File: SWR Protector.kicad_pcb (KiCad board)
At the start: 2 copper layers, 82.7 x 56.6 mm, 28 parts, among them J1 Barrel_Jack, J2 antenna, J3 Conn_02x03, J4 transceiver, J5 Barrel_Jack, K1 ATX209, Q1 2N3904, T1 1:12, T2 1:12, U1 LM78L05_TO92, U2 LM358

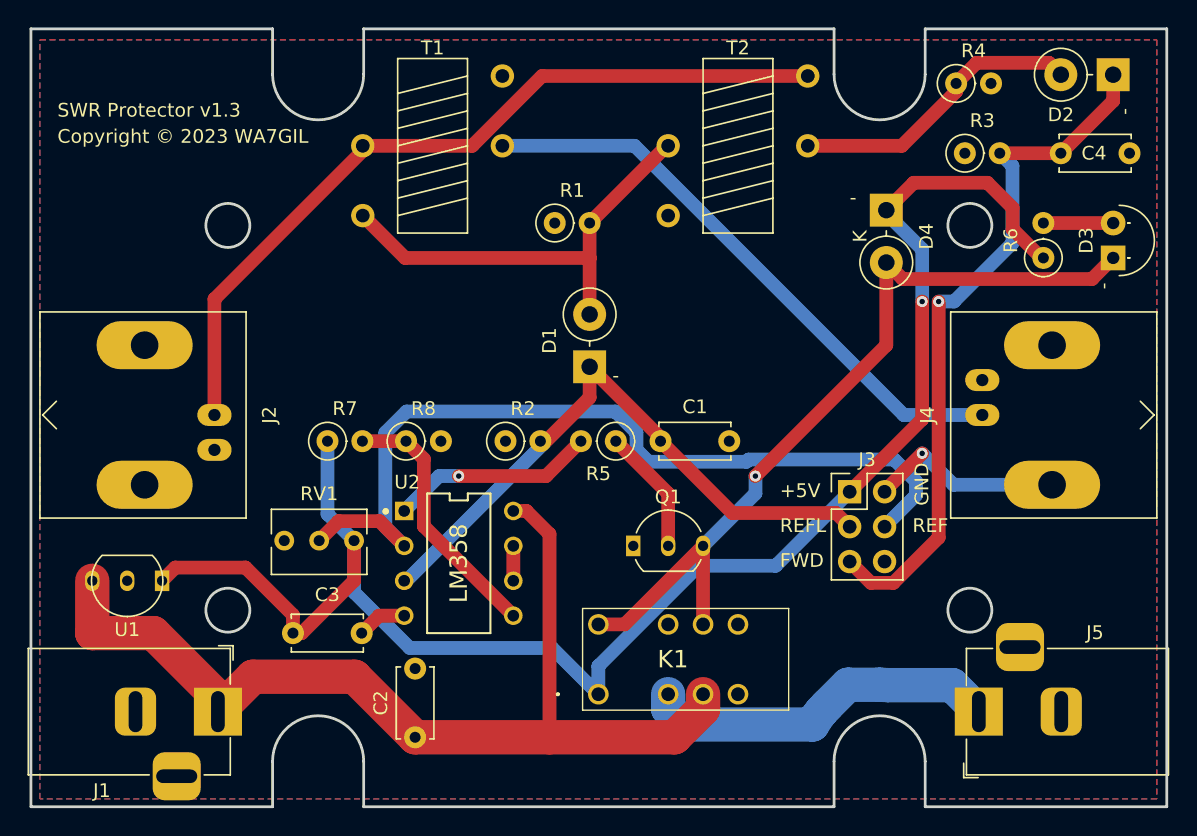
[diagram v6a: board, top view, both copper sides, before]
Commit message: The George Option complete. George asked for a buzzer when relay trips.  Used 12V part w/ same footprint. That thing is HUGE.  I can see already I want a jumper to disable it after I build one to test.
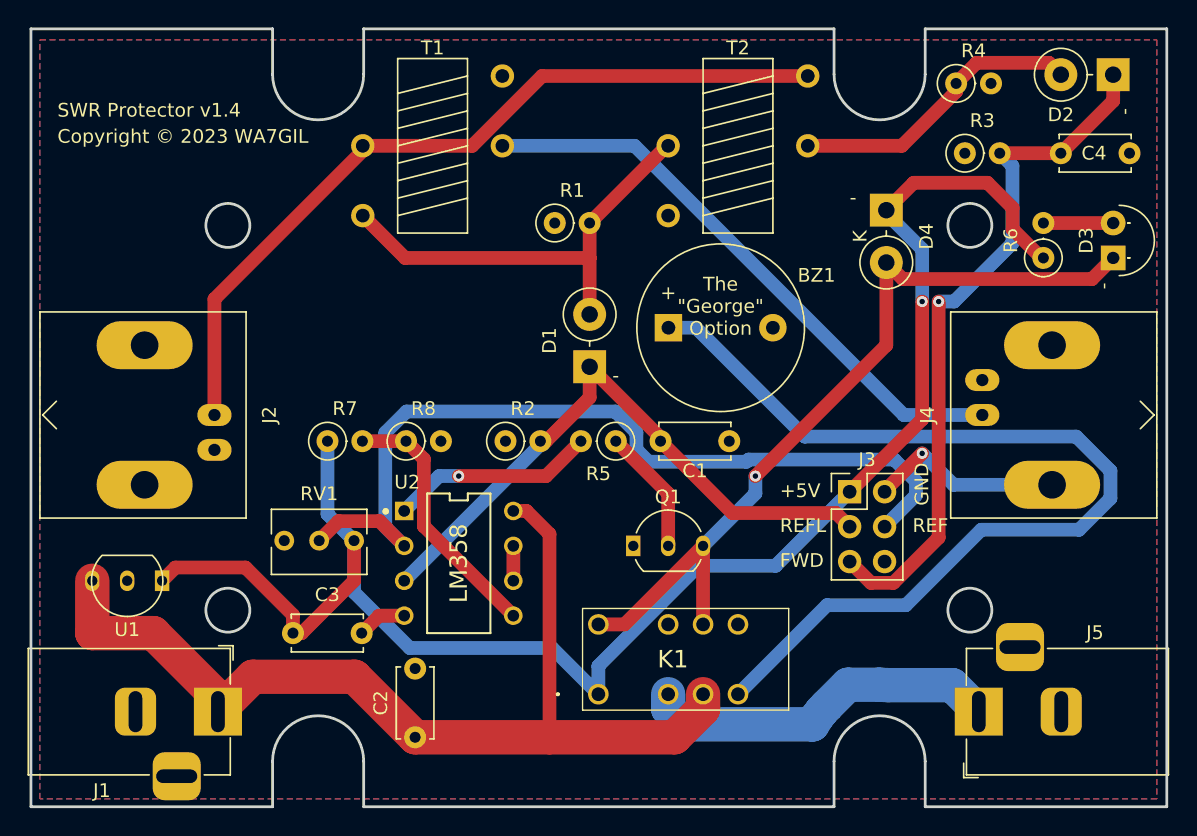
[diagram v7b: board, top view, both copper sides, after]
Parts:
- added BZ1: Buzzer, Buzzer_Beeper:Buzzer_12x9.5RM7.6, F.Cu at (160.0, 96.5)
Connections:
- K1 pad 5: unconnected-(K1-NO_1-Pad5) -> Net-(BZ1--)
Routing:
- net Net-(BZ1--): track 0.00 -> 71.5 mm
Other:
- board text added: "SWR Protector v1.4"
- board text added: "The {dblquote}George{dblquote} Option"
- board text removed: "SWR Protector v1.3"

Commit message: add jumper to disable George buzzer
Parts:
- added J6: Conn_01x02_Pin, Connector_PinHeader_2.54mm:PinHeader_1x02_P2.54mm_Vertical, F.Cu at (172.7, 104.1)
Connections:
- K1 pad 5: Net-(BZ1--) -> Net-(J6-Pin_2)
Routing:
- net Net-(BZ1--): track 71.5 -> 15.8 mm
- net Net-(J6-Pin_2): track 0.00 -> 53.1 mm
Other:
- board text added: "SWR Protector v1.5"
- board text removed: "SWR Protector v1.4"
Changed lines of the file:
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@@
     (title "SWR Protector WA7GIL")
     (date "2023-05-28")
-    (rev "v1.4")
+    (rev "v1.5")
   )
   (layers
@@
   (net 19 "unconnected-(J3-Pin_6-Pad6)")
   (net 20 "Net-(BZ1--)")
+  (net 21 "Net-(J6-Pin_2)")
   (footprint "Capacitor_THT:C_Disc_D5.0mm_W2.5mm_P5.00mm" (layer "F.Cu")
     (at 188.595 83.82)
@@
       (net 5 "+12V") (pinfunction "COM_1") (pintype "passive"))
     (pad "5" thru_hole circle (at 10.16 0) (size 1.5 1.5) (drill 1) (layers "*.Cu" "*.Mask")
-      (net 20 "Net-(BZ1--)") (pinfunction "NO_1") (pintype "passive"))
+      (net 21 "Net-(J6-Pin_2)") (pinfunction "NO_1") (pintype "passive"))
     (pad "8" thru_hole circle (at 10.16 -5.08) (size 1.5 1.5) (drill 1) (layers "*.Cu" "*.Mask")
       (net 2 "GND") (pinfunction "NO_2") (pintype "passive"))
@@
       (net 10 "Net-(J2-In)") (pinfunction "SB") (pintype "passive"))
   )
+  (footprint "Connector_PinHeader_2.54mm:PinHeader_1x02_P2.54mm_Vertical" (layer "F.Cu")
+    (at 172.715 104.14 90)
+    (descr "Through hole straight pin header, 1x02, 2.54mm pitch, single row")
+    (tags "Through hole pin header THT 1x02 2.54mm single row")
+    (property "Sheetfile" "SWR Protector.kicad_sch")
+    (property "Sheetname" "")
+    (property "ki_description" "Generic connector, single row, 01x02, script generated")
+    (property "ki_keywords" "connector")
+    (attr through_hole)
+    (fp_text reference "J6" (at 0 -2.33 90) (layer "F.SilkS")
+        (effects (font (size 1 1) (thickness 0.15)))
+    )
+    (fp_text value "Conn_01x02_Pin" (at 0 4.87 90) (layer "F.Fab")
+        (effects (font (size 1 1) (thickness 0.15)))
+    )
+    (fp_text user "${REFERENCE}" (at 0 1.27) (layer "F.Fab")
+        (effects (font (size 1 1) (thickness 0.15)))
+    )
+    (fp_line (start -1.33 -1.33) (end 0 -1.33)
+      (stroke (width 0.12) (type solid)) (layer "F.SilkS"))
+    (fp_line (start -1.33 0) (end -1.33 -1.33)
+      (stroke (width 0.12) (type solid)) (layer "F.SilkS"))
+    (fp_line (start -1.33 1.27) (end -1.33 3.87)
+      (stroke (width 0.12) (type solid)) (layer "F.SilkS"))
+    (fp_line (start -1.33 1.27) (end 1.33 1.27)
+      (stroke (width 0.12) (type solid)) (layer "F.SilkS"))
+    (fp_line (start -1.33 3.87) (end 1.33 3.87)
+      (stroke (width 0.12) (type solid)) (layer "F.SilkS"))
+    (fp_line (start 1.33 1.27) (end 1.33 3.87)
+      (stroke (width 0.12) (type solid)) (layer "F.SilkS"))
+    (fp_line (start -1.8 -1.8) (end -1.8 4.35)
+      (stroke (width 0.05) (type solid)) (layer "F.CrtYd"))
+    (fp_line (start -1.8 4.35) (end 1.8 4.35)
+      (stroke (width 0.05) (type solid)) (layer "F.CrtYd"))
+    (fp_line (start 1.8 -1.8) (end -1.8 -1.8)
+      (stroke (width 0.05) (type solid)) (layer "F.CrtYd"))
+    (fp_line (start 1.8 4.35) (end 1.8 -1.8)
+      (stroke (width 0.05) (type solid)) (layer "F.CrtYd"))
+    (fp_line (start -1.27 -0.635) (end -0.635 -1.27)
+      (stroke (width 0.1) (type solid)) (layer "F.Fab"))
+    (fp_line (start -1.27 3.81) (end -1.27 -0.635)
+      (stroke (width 0.1) (type solid)) (layer "F.Fab"))
+    (fp_line (start -0.635 -1.27) (end 1.27 -1.27)
+      (stroke (width 0.1) (type solid)) (layer "F.Fab"))
+    (fp_line (start 1.27 -1.27) (end 1.27 3.81)
+      (stroke (width 0.1) (type solid)) (layer "F.Fab"))
+    (fp_line (start 1.27 3.81) (end -1.27 3.81)
+      (stroke (width 0.1) (type solid)) (layer "F.Fab"))
+    (pad "1" thru_hole rect (at 0 0 90) (size 1.7 1.7) (drill 1) (layers "*.Cu" "*.Mask")
+      (net 20 "Net-(BZ1--)") (pinfunction "Pin_1") (pintype "passive"))
+    (pad "2" thru_hole oval (at 0 2.54 90) (size 1.7 1.7) (drill 1) (layers "*.Cu" "*.Mask")
+      (net 21 "Net-(J6-Pin_2)") (pinfunction "Pin_2") (pintype "passive"))
+    (model "${KICAD6_3DMODEL_DIR}/Connector_PinHeader_2.54mm.3dshapes/PinHeader_1x02_P2.54mm_Vertical.wrl"
+      (offset (xyz 0 0 0))
+      (scale (xyz 1 1 1))
+      (rotate (xyz 0 0 0))
+    )
+  )
   (footprint "Resistor_THT:R_Axial_DIN0207_L6.3mm_D2.5mm_P2.54mm_Vertical" (layer "F.Cu")
     (at 148.18 104.775)
@@
     (fp_arc (start 1.27 -2.601326) (mid 2.690476 -2.179253) (end 3.649999 -1.05)
       (stroke (width 0.12) (type solid)) (layer "F.SilkS"))
-    (fp_arc (start 3.649999 1) (mid 3.412642 1.435599) (end 3.096913 1.818222)
+    (fp_arc (start 3.649999 1) (mid 3.412641 1.435598) (end 3.096913 1.818222)
       (stroke (width 0.12) (type solid)) (layer "F.SilkS"))
     (fp_line (start -1.46 -2.73) (end -1.46 2.01)
@@
     (property "ki_keywords" "connector")
     (attr through_hole)
-    (fp_text reference "J3" (at 1.27 -2.33) (layer "F.SilkS")
+    (fp_text reference "J3" (at 1.397 7.112) (layer "F.SilkS")
         (effects (font (size 1 1) (thickness 0.15)))
     )
@@
     (effects (font (size 1 1) (thickness 0.15)) (justify left bottom))
   )
-  (gr_text "SWR Protector v1.4" (at 115.57 81.28) (layer "F.SilkS")
+  (gr_text "SWR Protector v1.5" (at 115.57 81.28) (layer "F.SilkS")
     (effects (font (size 1 1) (thickness 0.15)) (justify left bottom))
   )
@@
   (segment (start 144.78 107.315) (end 143.35 107.315) (width 1) (layer "B.Cu") (net 17))
   (segment (start 148.75 114.935) (end 148.75 112.395) (width 1) (layer "F.Cu") (net 18))
-  (segment (start 171.5792 116.7108) (end 177.3182 116.7108) (width 1) (layer "B.Cu") (net 20))
-  (segment (start 192.2072 106.9336) (end 189.7164 104.4428) (width 1) (layer "B.Cu") (net 20))
-  (segment (start 160.04 96.52) (end 162.04 96.52) (width 1) (layer "B.Cu") (net 20))
-  (segment (start 169.9628 104.4428) (end 162.04 96.52) (width 1) (layer "B.Cu") (net 20))
-  (segment (start 165.1 123.19) (end 171.5792 116.7108) (width 1) (layer "B.Cu") (net 20))
-  (segment (start 189.9268 111.2205) (end 192.2072 108.9401) (width 1) (layer "B.Cu") (net 20))
-  (segment (start 177.3182 116.7108) (end 182.8085 111.2205) (width 1) (layer "B.Cu") (net 20))
-  (segment (start 189.7164 104.4428) (end 169.9628 104.4428) (width 1) (layer "B.Cu") (net 20))
-  (segment (start 192.2072 108.9401) (end 192.2072 106.9336) (width 1) (layer "B.Cu") (net 20))
-  (segment (start 182.8085 111.2205) (end 189.9268 111.2205) (width 1) (layer "B.Cu") (net 20))
+  (segment (start 167.66 104.14) (end 160.04 96.52) (width 1) (layer "B.Cu") (net 20))
+  (segment (start 172.715 104.14) (end 167.66 104.14) (width 1) (layer "B.Cu") (net 20))
+  (segment (start 171.5792 116.7108) (end 165.1 123.19) (width 1) (layer "B.Cu") (net 21))
+  (segment (start 192.2072 106.9336) (end 192.2072 108.9401) (width 1) (layer "B.Cu") (net 21))
+  (segment (start 175.255 104.14) (end 175.485 104.37) (width 1) (layer "B.Cu") (net 21))
+  (segment (start 192.2072 108.9401) (end 189.9268 111.2205) (width 1) (layer "B.Cu") (net 21))
+  (segment (start 175.485 104.37) (end 189.6436 104.37) (width 1) (layer "B.Cu") (net 21))
+  (segment (start 177.3182 116.7108) (end 171.5792 116.7108) (width 1) (layer "B.Cu") (net 21))
+  (segment (start 182.8085 111.2205) (end 177.3182 116.7108) (width 1) (layer "B.Cu") (net 21))
+  (segment (start 189.9268 111.2205) (end 182.8085 111.2205) (width 1) (layer "B.Cu") (net 21))
+  (segment (start 189.6436 104.37) (end 192.2072 106.9336) (width 1) (layer "B.Cu") (net 21))
   (zone (net 2) (net_name "GND") (layer "F.Cu") (hatch edge 0.5)
     (priority 1)
